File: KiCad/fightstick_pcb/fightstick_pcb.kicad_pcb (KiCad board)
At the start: 2 copper layers, 87.5 x 70.5 mm, 118 parts, among them J1 USB_B_Micro, J2 Conn_01x02, J3 Conn_01x02, J4 Screw_Terminal_01x12, J5 Screw_Terminal_01x12, J6 Screw_Terminal_01x12, SW1 SW_Push, U1 SN74LVC1G14DBV, U10 SN74LVC1G14DBV, U11 SN74LVC1G14DBV, U12 SN74LVC1G14DBV, U13 SN74LVC1G14DBV, U14 SN74LVC1G14DBV, U15 SN74LVC1G14DBV, U2 SN74LVC1G14DBV, U3 NCP1117-3.3_SOT223, U4 W25Q128JVS, U5 SN74LVC1G14DBV, U6 SN74LVC1G14DBV, U7 SN74LVC1G14DBV, U8 SN74LVC1G14DBV, U9 RP2040, Y1 ABM8-272-T3

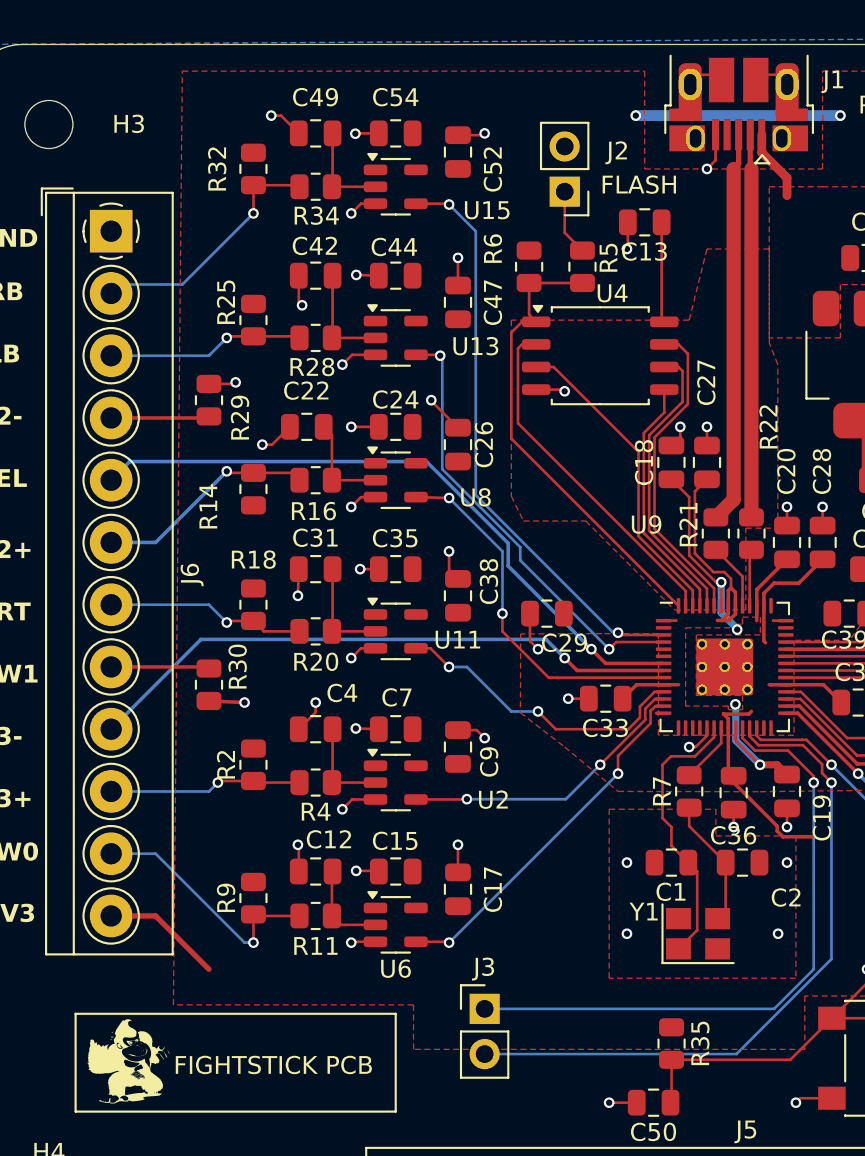
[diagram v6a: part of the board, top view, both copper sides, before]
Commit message: Trace GND du USB agrandie
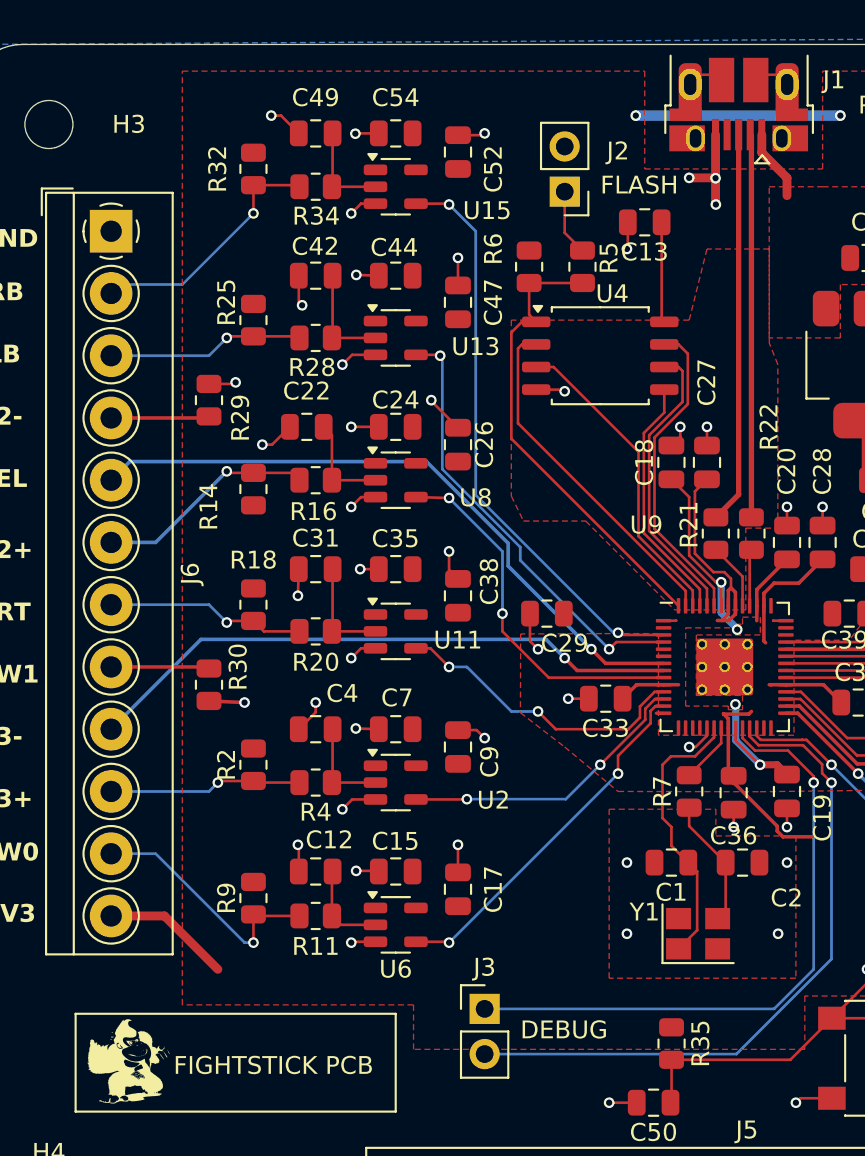
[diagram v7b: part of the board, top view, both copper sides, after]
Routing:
- net GND: track 130.3 -> 133.6 mm, vias 79 -> 81
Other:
- board text added: "DEBUG"
